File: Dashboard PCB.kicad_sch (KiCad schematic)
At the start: 35 parts, among them J4 CarCAN_ConnIn_01x02, J5 InternalCAN_ConnIn_01x02, J6 InternalCAN_ConnOut_01x02, J7 E_Stop_In_01x02, J8 CarCAN_ConnOut_01x02, J9 E_Stop_Out_01x02

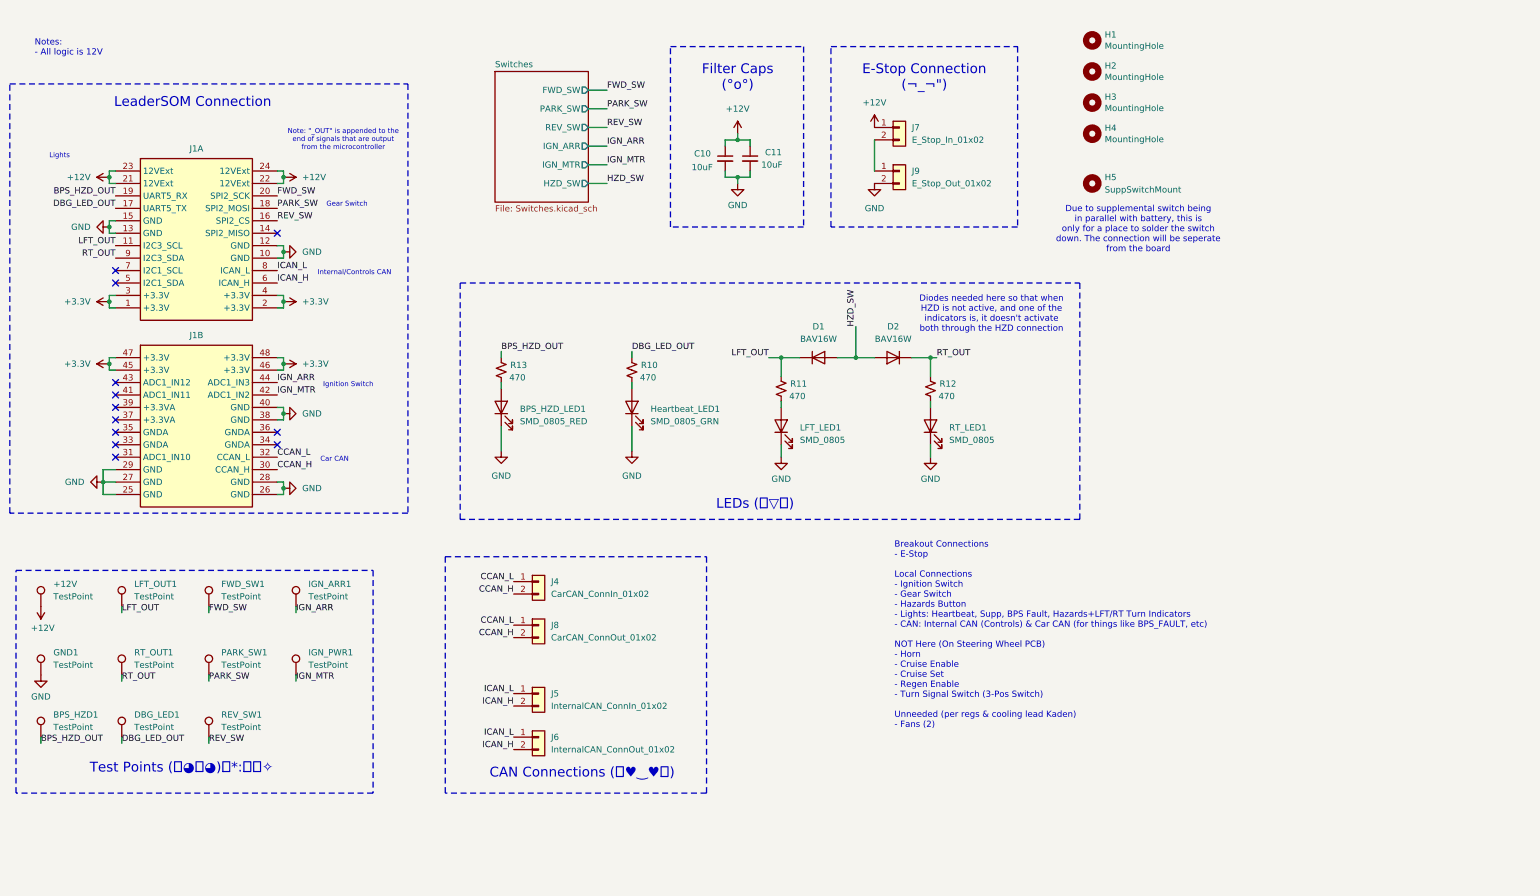
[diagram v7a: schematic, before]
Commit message: Changed from Internal CAN to Peripheral CAN
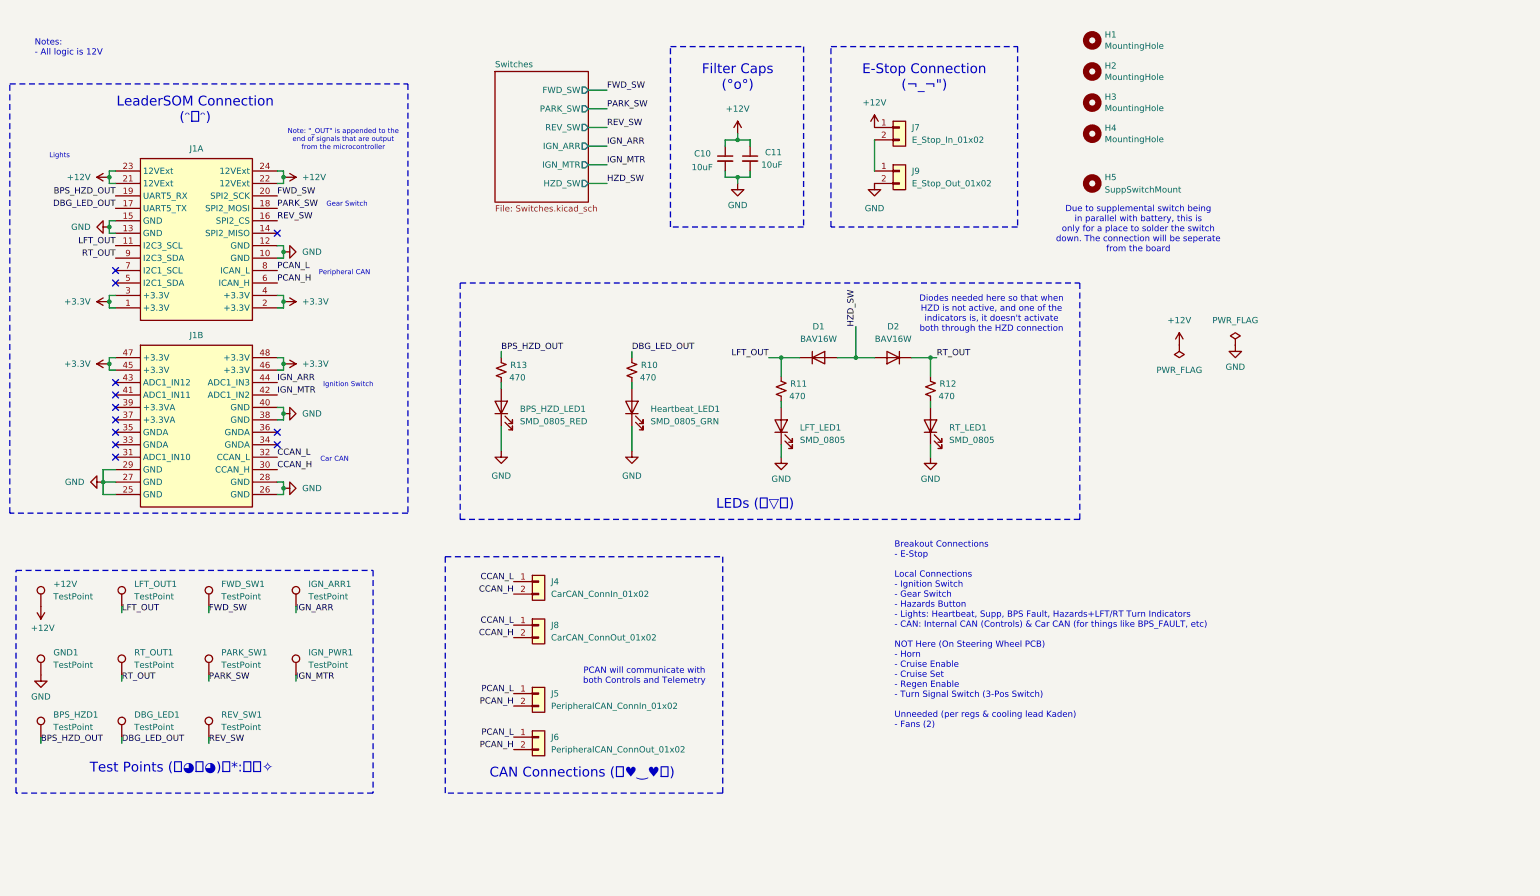
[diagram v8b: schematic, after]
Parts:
- J5: value InternalCAN_ConnIn_01x02 -> PeripheralCAN_ConnIn_01x02
- J6: value InternalCAN_ConnOut_01x02 -> PeripheralCAN_ConnOut_01x02
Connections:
- net ICAN_H renamed PCAN_H
- net ICAN_L renamed PCAN_L
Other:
- note added: "LeaderSOM Connection (ᵔᴥᵔ)"
- note added: "PCAN will communicate with both Controls and Telemetry"
- note added: "Peripheral CAN"
- note removed: "Internal/Controls CAN"
- note removed: "LeaderSOM Connection"
